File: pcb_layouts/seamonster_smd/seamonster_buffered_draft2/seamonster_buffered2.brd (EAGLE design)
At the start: 172.5 x 106.5 mm, 132 parts, among them IC1 7808DT, IC2 4051D, IC3 4051D, IC4 DG408DY, IC5 4046D, IC6 40106D, IC7 4070D, IC8 4046D, IC9 4040D, Q1 THONKICONNNEW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

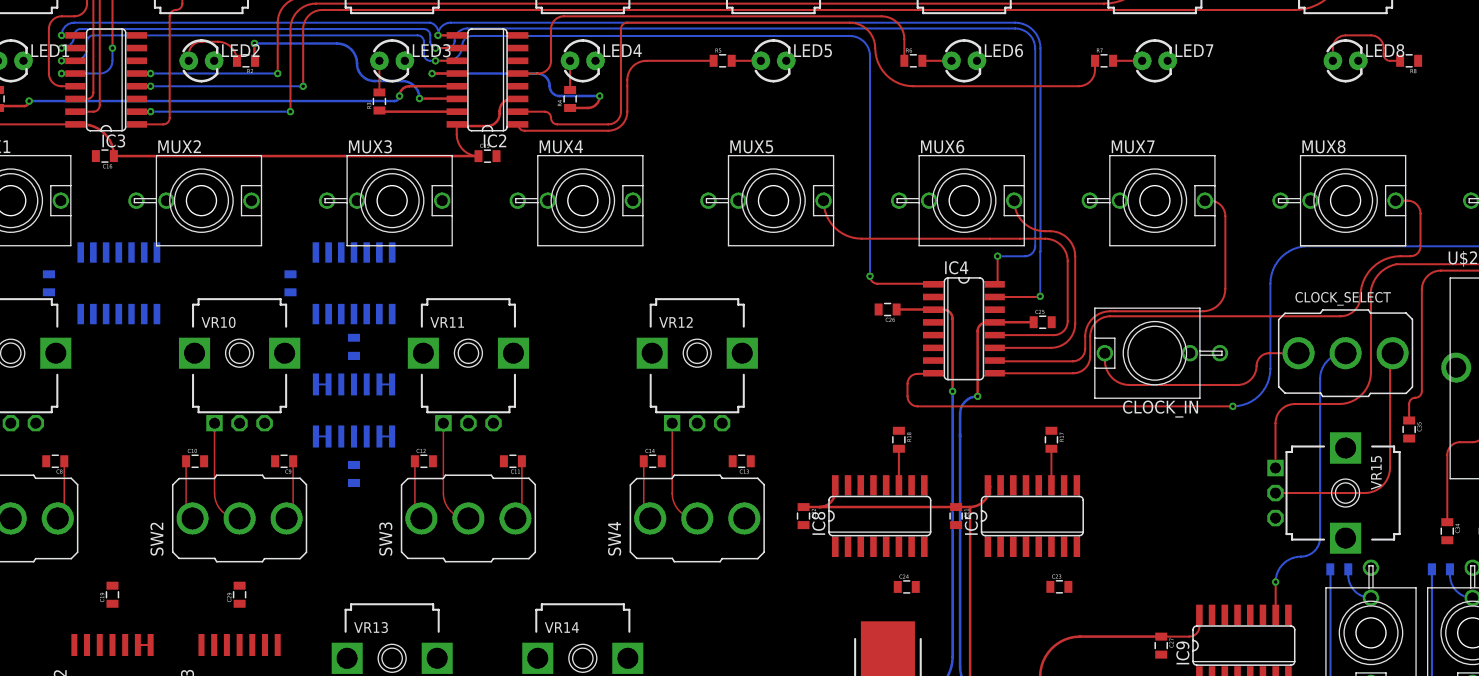
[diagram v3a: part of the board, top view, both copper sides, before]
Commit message: finished routing IO to DG408 MUX
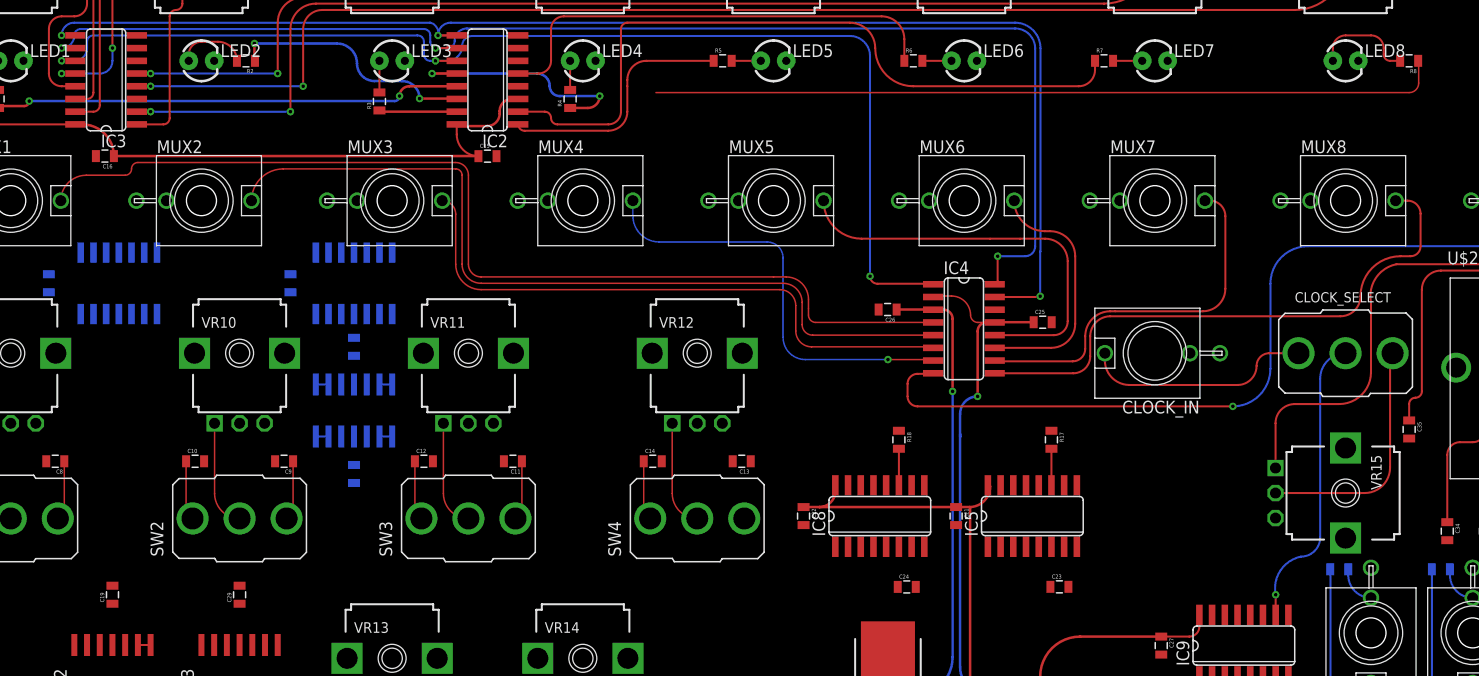
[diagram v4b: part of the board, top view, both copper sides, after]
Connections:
- net V+: now also IC4.2
- net VCC: no longer IC4.2
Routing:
- net MUX1: track 0.00 -> 101.5 mm
- net MUX2: track 0.00 -> 82.8 mm
- net N$26: track 0.00 -> 78.8 mm
- net MUX3: track 0.00 -> 59.6 mm
- net MUX4: track 0.00 -> 42.1 mm, vias 0 -> 1
- net V+: track 84.9 -> 91.3 mm
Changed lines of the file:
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@@
 <wire x1="105" y1="59" x2="105" y2="59.25" width="0.254" layer="16"/>
 <wire x1="106.75" y1="63" x2="106.75" y2="69.5" width="0.254" layer="1"/>
-<wire x1="106.75" y1="69.5" x2="107.635" y2="70.385" width="0.254" layer="1" curve="-90"/>
+<wire x1="107.635" y1="70.385" x2="106.75" y2="69.5" width="0.254" layer="1" curve="90"/>
 <wire x1="107.635" y1="70.385" x2="108.4534" y2="70.385" width="0.254" layer="1"/>
 <wire x1="108.4534" y1="70.385" x2="108.4734" y2="70.405" width="0.254" layer="1" curve="-90"/>
@@
 <wire x1="106.75" y1="63" x2="105" y2="61.25" width="0.254" layer="16" curve="90"/>
 <wire x1="105" y1="61.25" x2="105" y2="59" width="0.254" layer="16"/>
+<contactref element="IC4" pad="2"/>
+<wire x1="102.3066" y1="72.925" x2="102.4066" y2="73.025" width="0.1524" layer="1" curve="-90"/>
+<wire x1="102.4066" y1="73.025" x2="104.14" y2="73.025" width="0.1524" layer="1"/>
+<wire x1="104.14" y1="73.025" x2="106.045" y2="71.12" width="0.1524" layer="1" curve="-90"/>
+<wire x1="106.045" y1="71.12" x2="106.78" y2="70.385" width="0.1524" layer="1" curve="90"/>
+<wire x1="106.78" y1="70.385" x2="107.635" y2="70.385" width="0.1524" layer="1"/>
 <wire x1="44.45" y1="56.145" x2="92.975" y2="28.575" width="0" layer="19" extent="1-16"/>
 <wire x1="44.45" y1="58.995" x2="44.45" y2="56.145" width="0" layer="19" extent="16-16"/>
@@
 <contactref element="VR7" pad="3"/>
 <contactref element="VR8" pad="3"/>
-<contactref element="IC4" pad="2"/>
 <contactref element="IC9" pad="16"/>
 <contactref element="C27" pad="1"/>
@@
 <wire x1="106" y1="31.75" x2="104" y2="29.75" width="0.254" layer="1" curve="-90"/>
 <wire x1="106" y1="51.88" x2="106" y2="31.75" width="0.254" layer="1"/>
-<wire x1="107.775" y1="54.1134" x2="102.3066" y2="72.925" width="0" layer="19" extent="1-1"/>
-<wire x1="102.91" y1="113.68" x2="102.3066" y2="72.925" width="0" layer="19" extent="1-1"/>
+<wire x1="56.885" y1="86.995" x2="89.36" y2="51.94" width="0" layer="19" extent="1-1"/>
 <wire x1="13.97" y1="73.395" x2="20.465" y2="87.005" width="0" layer="19" extent="1-16"/>
 <wire x1="17.145" y1="71.2216" x2="13.97" y2="73.395" width="0" layer="19" extent="16-16"/>
@@
 <contactref element="MUX1" pad="P$1_TIP"/>
 <contactref element="IC4" pad="4"/>
-<wire x1="15.16" y1="82.55" x2="102.3066" y2="70.385" width="0" layer="19" extent="1-1"/>
+<wire x1="15.16" y1="82.55" x2="17.7" y2="85.09" width="0.1524" layer="1" curve="-90"/>
+<wire x1="21.59" y1="85.09" x2="22.225" y2="85.725" width="0.1524" layer="1" curve="90"/>
+<wire x1="22.225" y1="85.725" x2="22.86" y2="86.36" width="0.1524" layer="1" curve="-90"/>
+<wire x1="17.7" y1="85.09" x2="21.59" y2="85.09" width="0.1524" layer="1"/>
+<wire x1="22.86" y1="86.36" x2="54.61" y2="86.36" width="0.1524" layer="1"/>
+<wire x1="54.61" y1="86.36" x2="55.88" y2="85.09" width="0.1524" layer="1" curve="-90"/>
+<wire x1="55.88" y1="76.2" x2="57.15" y2="74.93" width="0.1524" layer="1" curve="90"/>
+<wire x1="55.88" y1="85.09" x2="55.88" y2="76.2" width="0.1524" layer="1"/>
+<wire x1="57.15" y1="74.93" x2="86.36" y2="74.93" width="0.1524" layer="1"/>
+<wire x1="86.36" y1="74.93" x2="87.63" y2="74.93" width="0.1524" layer="1"/>
+<wire x1="87.63" y1="74.93" x2="89.8525" y2="72.7075" width="0.1524" layer="1" curve="-90"/>
+<wire x1="89.8525" y1="72.7075" x2="89.8525" y2="71.755" width="0.1524" layer="1"/>
+<wire x1="89.8525" y1="71.755" x2="89.8525" y2="71.12" width="0.1524" layer="1"/>
+<wire x1="89.8525" y1="71.12" x2="90.5875" y2="70.385" width="0.1524" layer="1" curve="90"/>
+<wire x1="90.5875" y1="70.385" x2="102.3066" y2="70.385" width="0.1524" layer="1"/>
 </signal>
 <signal name="MUX2">
 <contactref element="MUX2" pad="P$1_TIP"/>
 <contactref element="IC4" pad="5"/>
-<wire x1="34.21" y1="82.55" x2="102.3066" y2="69.115" width="0" layer="19" extent="1-1"/>
+<wire x1="34.21" y1="82.55" x2="37.385" y2="85.725" width="0.1524" layer="1" curve="-90"/>
+<wire x1="37.385" y1="85.725" x2="54.61" y2="85.725" width="0.1524" layer="1"/>
+<wire x1="54.61" y1="85.725" x2="55.245" y2="85.09" width="0.1524" layer="1" curve="-90"/>
+<wire x1="55.245" y1="76.2" x2="57.15" y2="74.295" width="0.1524" layer="1" curve="90"/>
+<wire x1="55.245" y1="85.09" x2="55.245" y2="76.2" width="0.1524" layer="1"/>
+<wire x1="87.3125" y1="74.295" x2="89.2175" y2="72.39" width="0.1524" layer="1" curve="-90"/>
+<wire x1="89.2175" y1="70.1675" x2="90.27" y2="69.115" width="0.1524" layer="1" curve="90"/>
+<wire x1="90.27" y1="69.115" x2="102.3066" y2="69.115" width="0.1524" layer="1"/>
+<wire x1="57.15" y1="74.295" x2="87.3125" y2="74.295" width="0.1524" layer="1"/>
+<wire x1="89.2175" y1="72.39" x2="89.2175" y2="70.1675" width="0.1524" layer="1"/>
 </signal>
 <signal name="MUX3">
 <contactref element="MUX3" pad="P$1_TIP"/>
 <contactref element="IC4" pad="6"/>
-<wire x1="53.26" y1="82.55" x2="102.3066" y2="67.845" width="0" layer="19" extent="1-1"/>
+<wire x1="53.26" y1="82.55" x2="54.61" y2="81.2" width="0.1524" layer="1" curve="-90"/>
+<wire x1="54.61" y1="76.2" x2="57.15" y2="73.66" width="0.1524" layer="1" curve="90"/>
+<wire x1="54.61" y1="81.2" x2="54.61" y2="76.2" width="0.1524" layer="1"/>
+<wire x1="86.995" y1="73.66" x2="88.5825" y2="72.0725" width="0.1524" layer="1" curve="-90"/>
+<wire x1="88.5825" y1="72.0725" x2="88.5825" y2="69.5325" width="0.1524" layer="1"/>
+<wire x1="88.5825" y1="69.5325" x2="90.17" y2="67.945" width="0.1524" layer="1" curve="90"/>
+<wire x1="90.17" y1="67.945" x2="102.2066" y2="67.945" width="0.1524" layer="1"/>
+<wire x1="102.2066" y1="67.945" x2="102.3066" y2="67.845" width="0.1524" layer="1" curve="-90"/>
+<wire x1="57.15" y1="73.66" x2="86.995" y2="73.66" width="0.1524" layer="1"/>
 </signal>
 <signal name="MUX4">
 <contactref element="MUX4" pad="P$1_TIP"/>
 <contactref element="IC4" pad="7"/>
-<wire x1="72.31" y1="82.55" x2="102.3066" y2="66.575" width="0" layer="19" extent="1-1"/>
+<wire x1="102.3066" y1="66.575" x2="102.2066" y2="66.675" width="0.1524" layer="1" curve="90"/>
+<via x="97.79" y="66.675" extent="1-16" drill="0.35"/>
+<wire x1="89.535" y1="66.675" x2="87.3125" y2="68.8975" width="0.1524" layer="16" curve="-90"/>
+<wire x1="87.3125" y1="76.835" x2="85.725" y2="78.4225" width="0.1524" layer="16" curve="90"/>
+<wire x1="74.93" y1="78.4225" x2="72.31" y2="81.0425" width="0.1524" layer="16" curve="-90"/>
+<wire x1="72.31" y1="81.0425" x2="72.31" y2="82.55" width="0.1524" layer="16"/>
+<wire x1="102.2066" y1="66.675" x2="97.79" y2="66.675" width="0.1524" layer="1"/>
+<wire x1="97.79" y1="66.675" x2="89.535" y2="66.675" width="0.1524" layer="16"/>
+<wire x1="87.3125" y1="68.8975" x2="87.3125" y2="76.835" width="0.1524" layer="16"/>
+<wire x1="85.725" y1="78.4225" x2="74.93" y2="78.4225" width="0.1524" layer="16"/>
 </signal>
 <signal name="MUX5">
@@
 <contactref element="R8" pad="1"/>
 <contactref element="IC2" pad="4"/>
-<wire x1="60.8584" y1="93.98" x2="150.76" y2="96.52" width="0" layer="19" extent="1-1"/>
+<wire x1="150.76" y1="96.52" x2="150.8125" y2="96.4675" width="0.1524" layer="1" curve="-90"/>
+<wire x1="150.8125" y1="94.2975" x2="149.86" y2="93.345" width="0.1524" layer="1" curve="-90"/>
+<wire x1="150.8125" y1="96.4675" x2="150.8125" y2="94.2975" width="0.1524" layer="1"/>
+<wire x1="149.86" y1="93.345" x2="74.6125" y2="93.345" width="0.1524" layer="1"/>
+<wire x1="60.8584" y1="93.98" x2="74.6125" y2="93.345" width="0" layer="19" extent="1-1"/>
 </signal>
 <signal name="N$18">
@@
 <contactref element="IC9" pad="10"/>
 <wire x1="143.51" y1="67.31" x2="140.97" y2="64.77" width="0.2032" layer="16" curve="90"/>
-<wire x1="140.97" y1="64.77" x2="140.97" y2="55.88" width="0.2032" layer="16"/>
-<wire x1="140.97" y1="55.88" x2="140.97" y2="49.53" width="0.2032" layer="16"/>
-<wire x1="140.97" y1="49.53" x2="140.97" y2="48.895" width="0.2032" layer="16"/>
+<wire x1="140.97" y1="64.77" x2="140.97" y2="48.895" width="0.2032" layer="16"/>
 <wire x1="140.97" y1="48.895" x2="139.065" y2="46.99" width="0.2032" layer="16" curve="-90"/>
-<wire x1="139.065" y1="46.99" x2="136.525" y2="44.45" width="0.2032" layer="16" curve="90"/>
-<via x="136.525" y="44.45" extent="1-16" drill="0.35"/>
-<wire x1="136.525" y1="44.45" x2="136.525" y2="41.1734" width="0.2032" layer="1"/>
+<wire x1="139.065" y1="46.99" x2="136.525" y2="43.18" width="0.2032" layer="16" curve="90"/>
+<via x="136.525" y="43.18" extent="1-16" drill="0.35"/>
+<wire x1="136.525" y1="43.18" x2="136.525" y2="41.1734" width="0.2032" layer="1"/>
 </signal>
 <signal name="Q1">
